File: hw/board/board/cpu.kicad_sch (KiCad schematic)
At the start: 1 part, among them U7 W65C02P

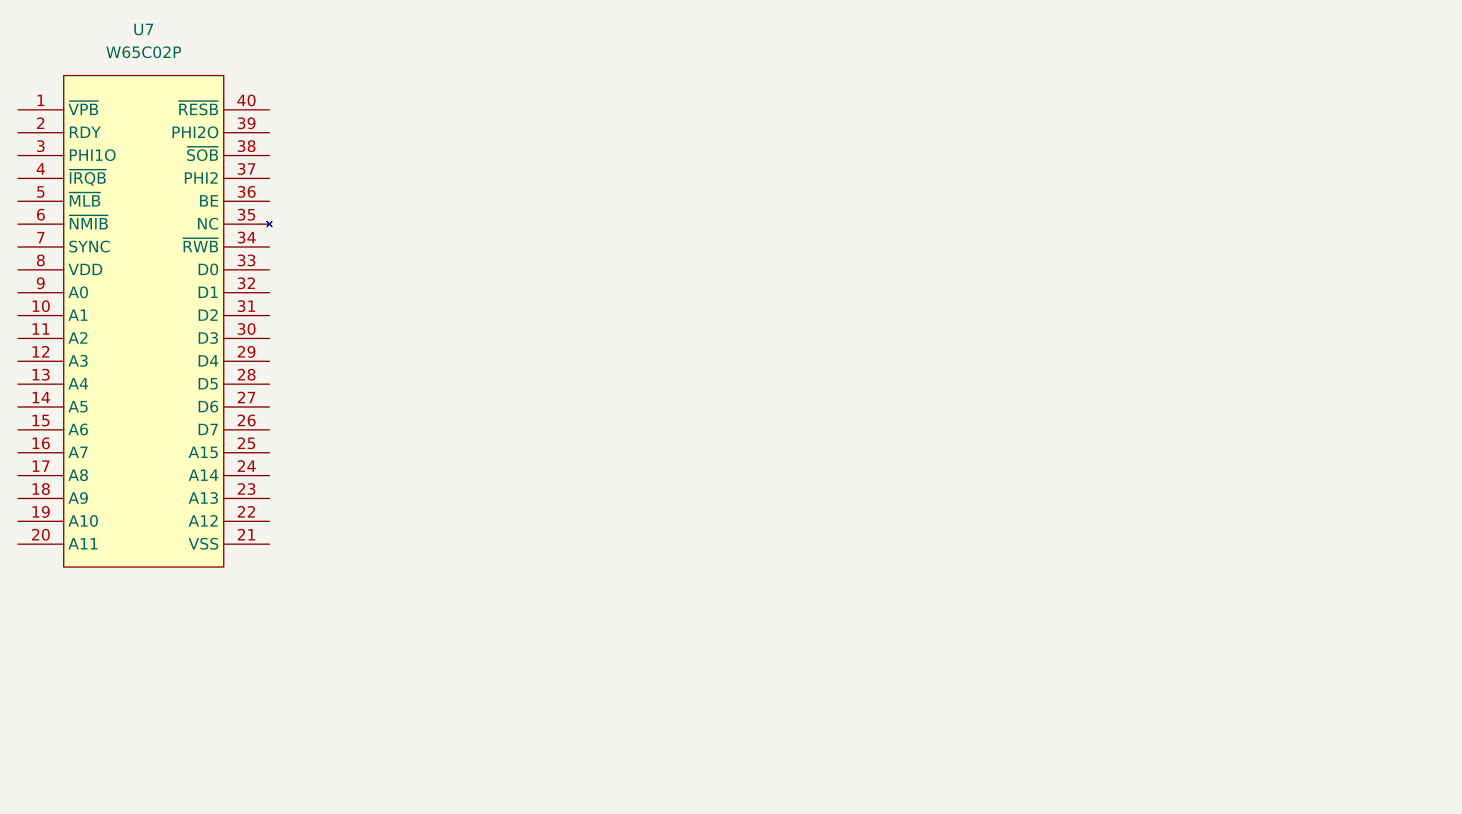
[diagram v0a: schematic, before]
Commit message: Add wires to fpga block (but don't connect them)
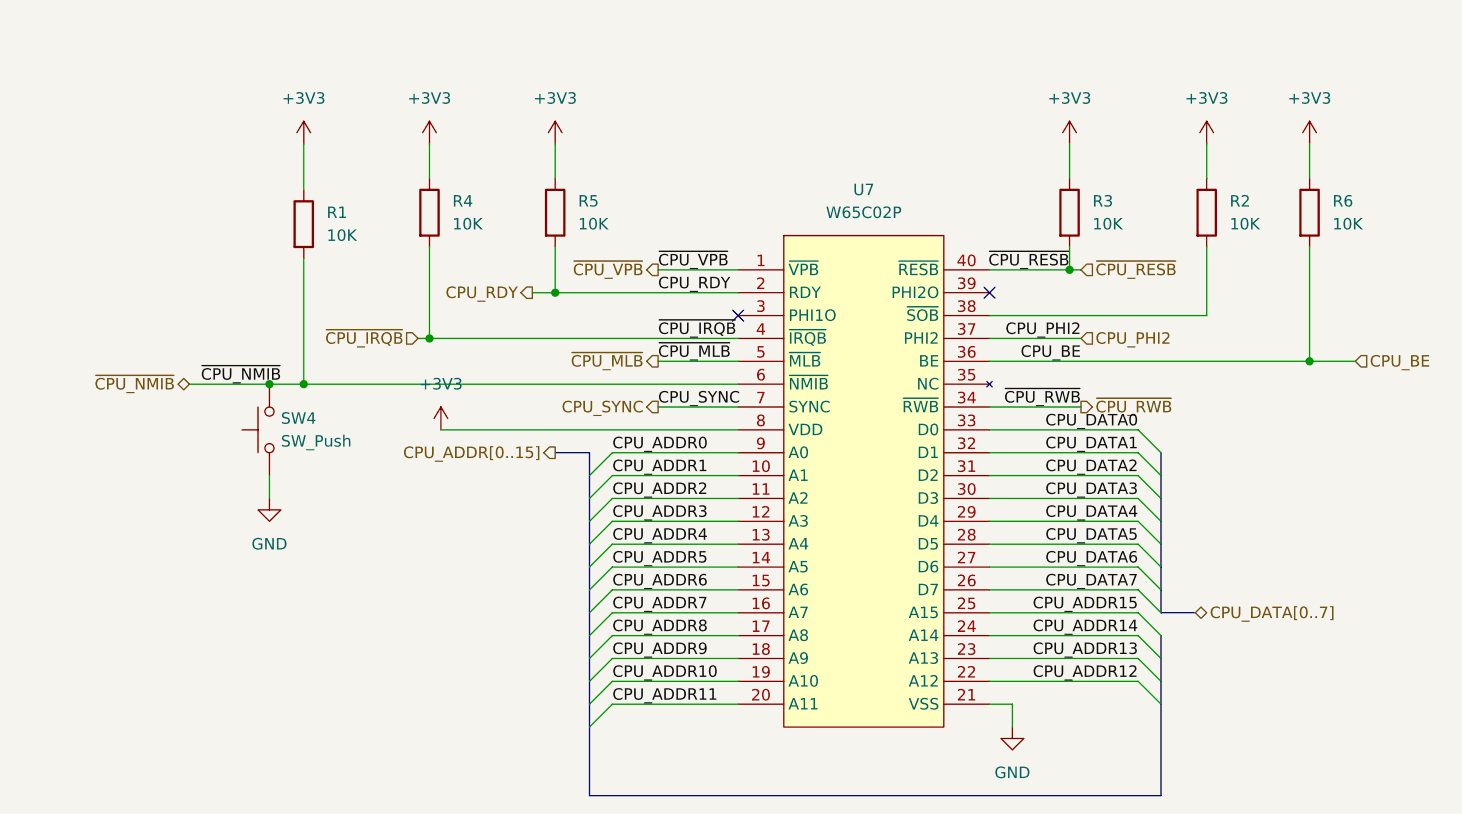
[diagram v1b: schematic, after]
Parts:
- added R1, R2, R3, R4, R5, R6: 10K, Resistor_SMD:R_0603_1608Metric_Pad0.98x0.95mm_HandSolder, symbol Device:R
- added SW4: SW_Push, Button_Switch_THT:SW_PUSH_6mm_H5mm, symbol Switch:SW_Push
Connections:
- net ~{CPU_VPB}: now reaches U7.1 (~{VPB})
- net CPU_ADDR1: now reaches U7.10 (A1)
- net CPU_ADDR2: now reaches U7.11 (A2)
- net CPU_ADDR3: now reaches U7.12 (A3)
- net CPU_ADDR4: now reaches U7.13 (A4)
- net CPU_ADDR5: now reaches U7.14 (A5)
- net CPU_ADDR6: now reaches U7.15 (A6)
- net CPU_ADDR7: now reaches U7.16 (A7)
- net CPU_ADDR8: now reaches U7.17 (A8)
- net CPU_ADDR9: now reaches U7.18 (A9)
- net CPU_ADDR10: now reaches U7.19 (A10)
- net CPU_RDY: now reaches U7.2 (RDY)
- net CPU_RDY: now also R5.2
- net CPU_ADDR11: now reaches U7.20 (A11)
- net GND: now reaches U7.21 (VSS)
- net GND: now also SW4.1
- net CPU_ADDR12: now reaches U7.22 (A12)
- net CPU_ADDR13: now reaches U7.23 (A13)
- net CPU_ADDR14: now reaches U7.24 (A14)
- net CPU_ADDR15: now reaches U7.25 (A15)
- net CPU_DATA7: now reaches U7.26 (D7)
- net CPU_DATA6: now reaches U7.27 (D6)
- net CPU_DATA5: now reaches U7.28 (D5)
- net CPU_DATA4: now reaches U7.29 (D4)
- net CPU_DATA3: now reaches U7.30 (D3)
- net CPU_DATA2: now reaches U7.31 (D2)
- net CPU_DATA1: now reaches U7.32 (D1)
- net CPU_DATA0: now reaches U7.33 (D0)
- net ~{CPU_RWB}: now reaches U7.34 (~{RWB})
- net CPU_BE: now reaches U7.36 (BE)
- net CPU_BE: now also R6.2
- net CPU_PHI2: now reaches U7.37 (PHI2)
- net at U7.38 (~{SOB}): now also R2.2
- net ~{CPU_IRQB}: now reaches U7.4 (~{IRQB})
- net ~{CPU_IRQB}: now also R4.2
- net ~{CPU_RESB}: now reaches U7.40 (~{RESB})
- net ~{CPU_RESB}: now also R3.2
- net ~{CPU_MLB}: now reaches U7.5 (~{MLB})
- net ~{CPU_NMIB}: now reaches U7.6 (~{NMIB})
- net ~{CPU_NMIB}: now also R1.2, SW4.2
- net CPU_SYNC: now reaches U7.7 (SYNC)
- net +3V3: now reaches U7.8 (VDD)
- net +3V3: now also R1.1, R2.1, R3.1, R4.1, R5.1, R6.1
- net CPU_ADDR0: now reaches U7.9 (A0)
- no-connect marks 0 -> 2
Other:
- moved on the sheet: U7
